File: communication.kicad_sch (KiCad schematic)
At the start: 17 parts, among them IC11 nRF52832-QFAA-R7, Y1 32MHz

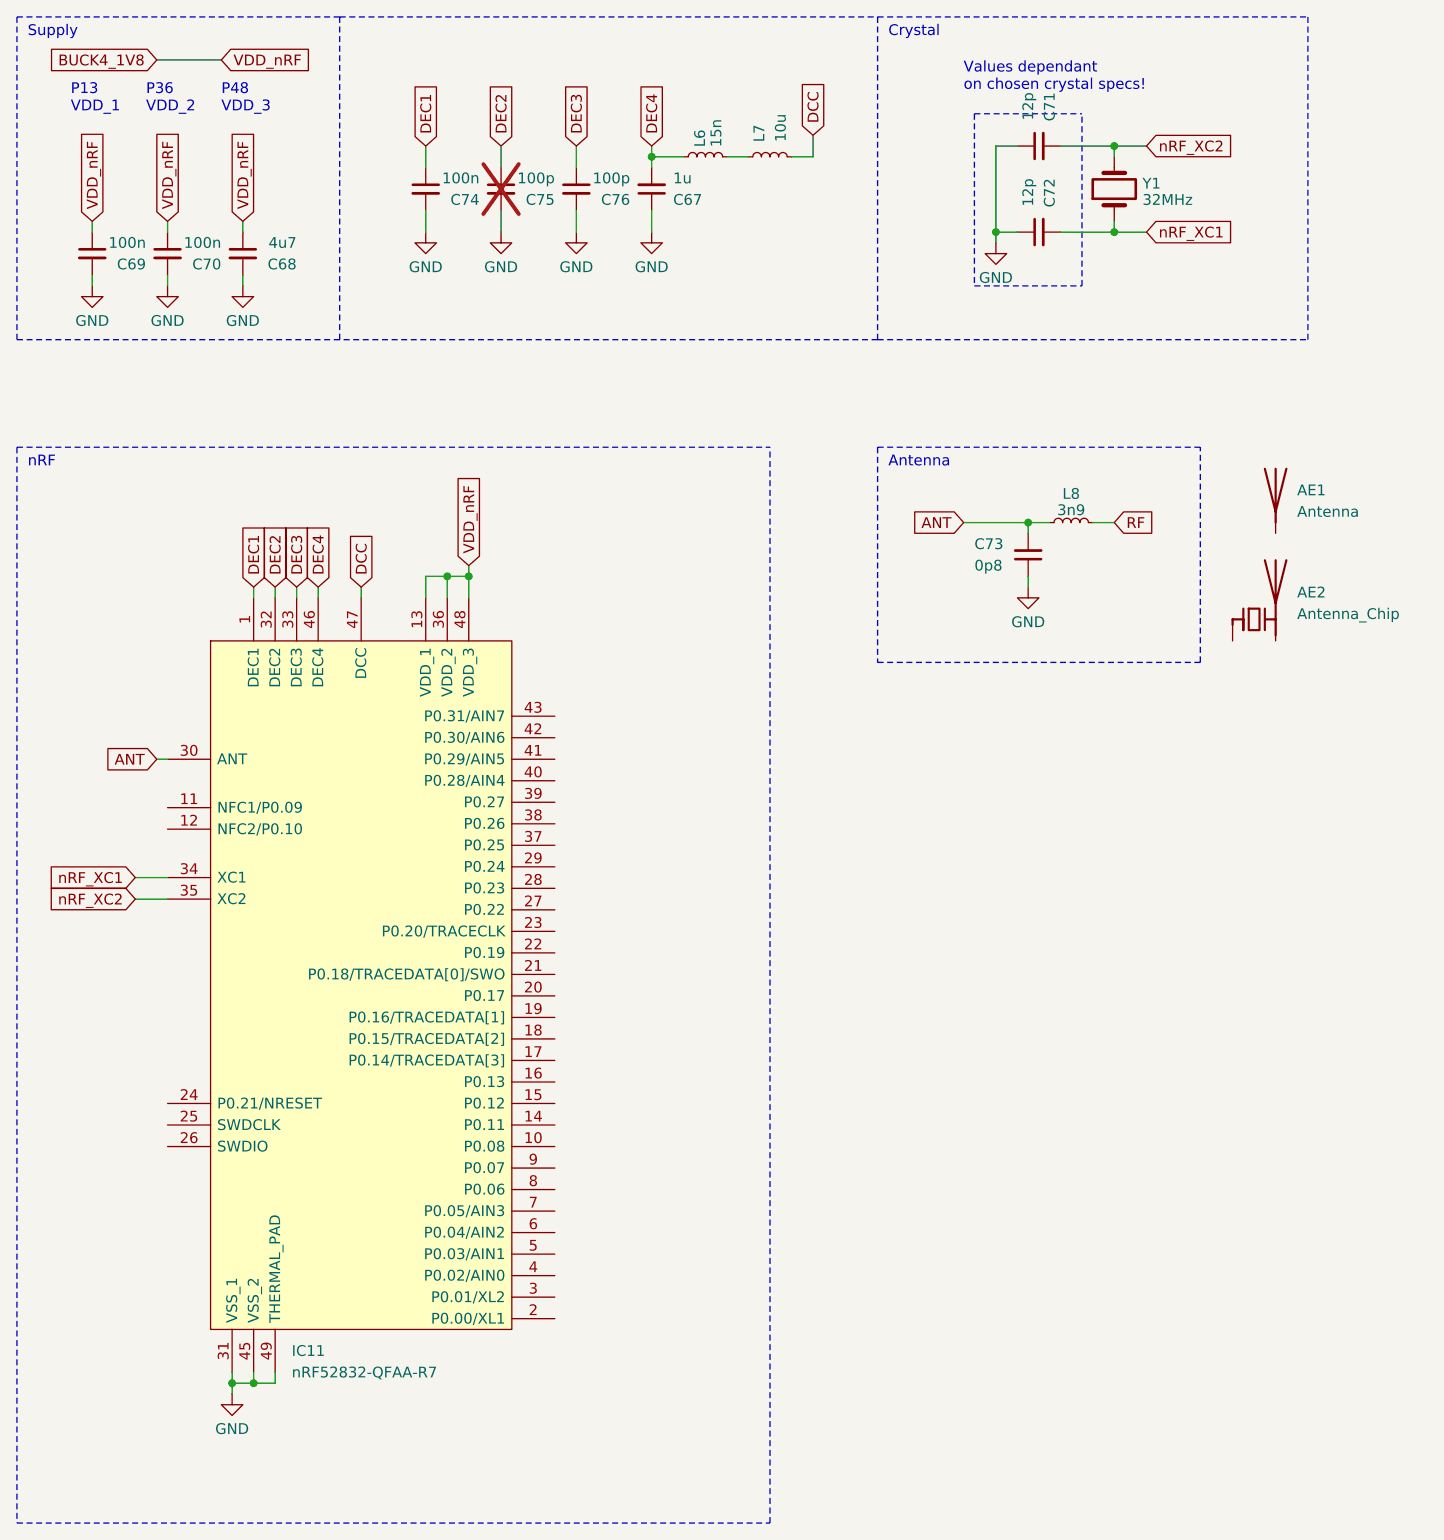
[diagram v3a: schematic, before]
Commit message: Added power to murata 1YN
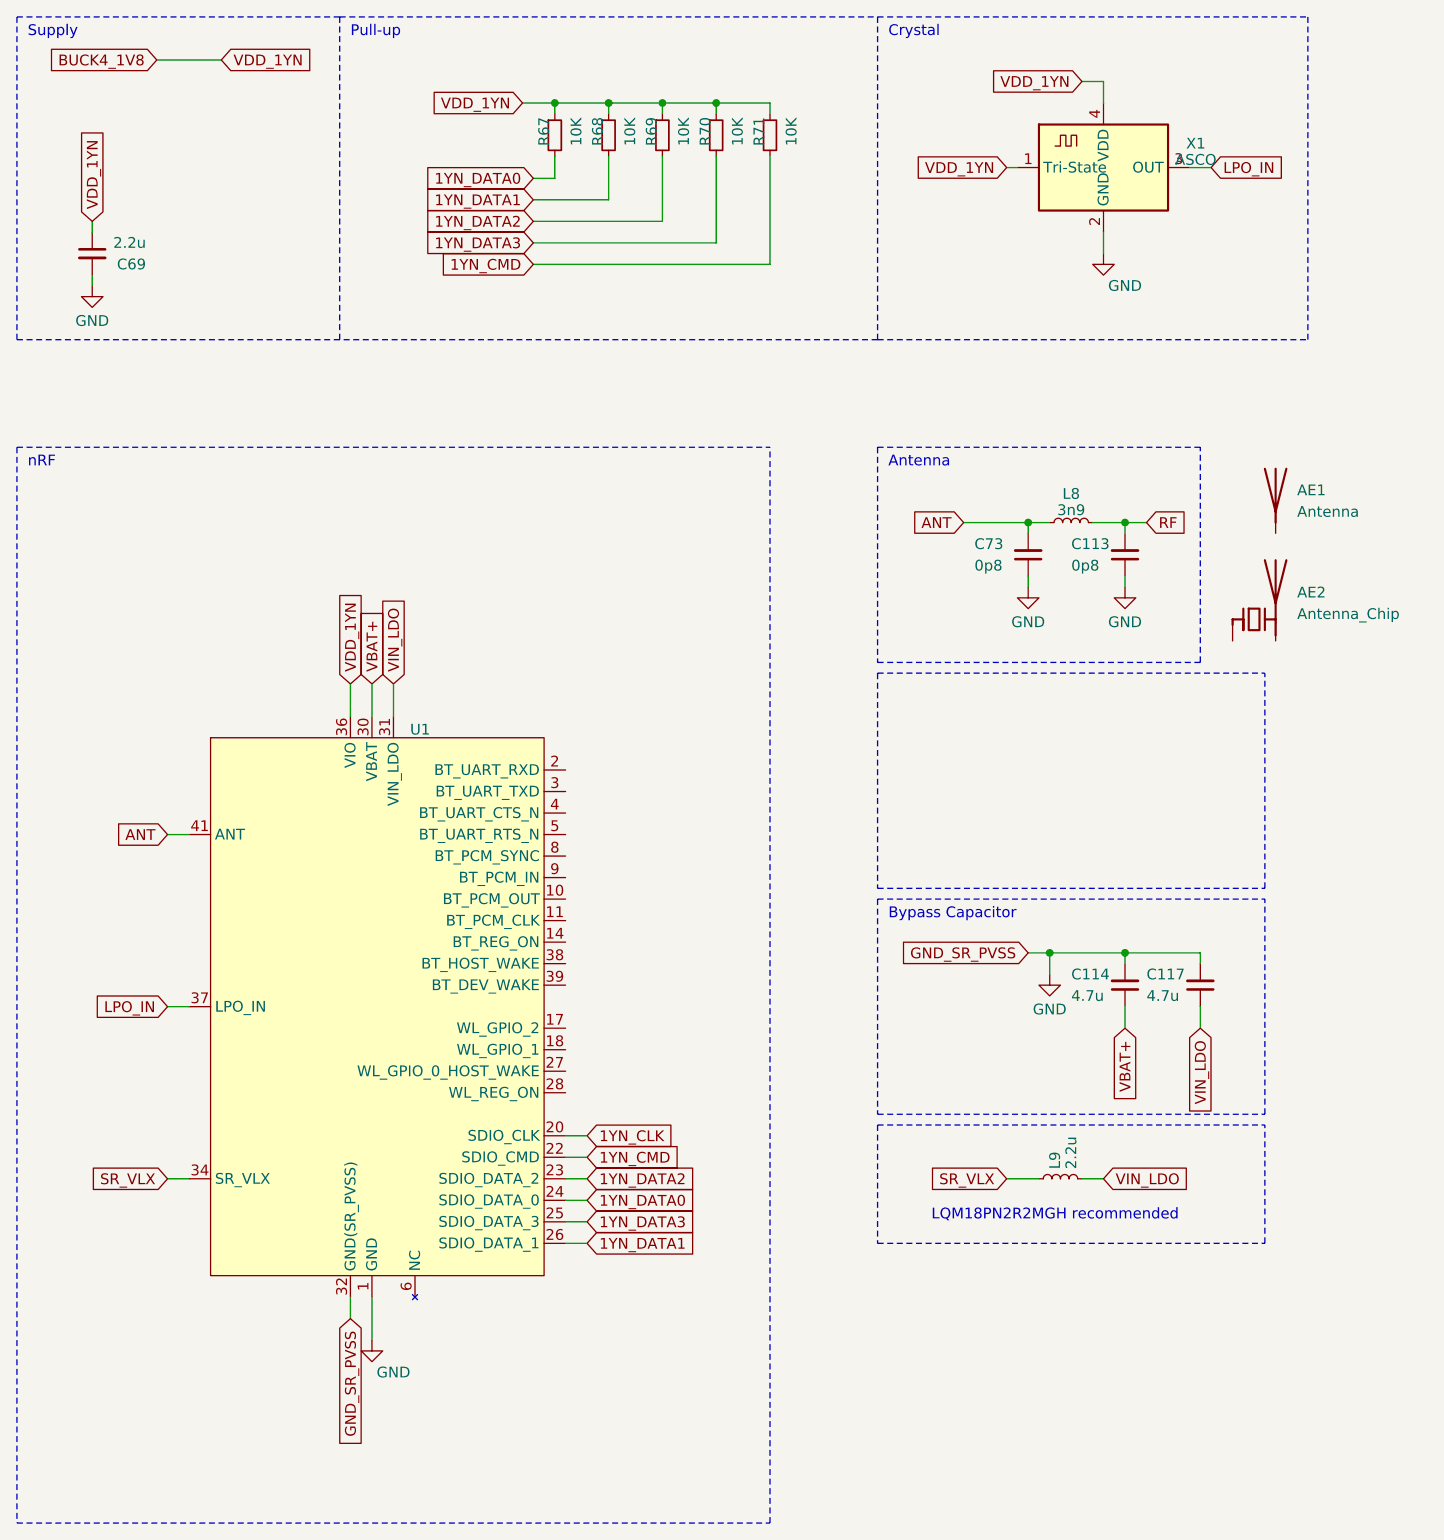
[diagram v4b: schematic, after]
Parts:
- removed C67: 1u, symbol Device:C_Small
- removed C68: 4u7, symbol Device:C_Small
- removed C70, C74: 100n, symbol Device:C_Small
- removed C71, C72: 12p, symbol Device:C_Small
- removed C75, C76: 100p, symbol Device:C_Small
- removed IC11: nRF52832-QFAA-R7, QFN40P600X600X90-49N-D, symbol ARMband:nRF52832-QFAA-R7
- removed L6: 15n, symbol Device:L_Small
- removed L7: 10u, symbol Device:L_Small
- removed Y1: 32MHz, symbol Device:Crystal
- added C113: 0p8, symbol Device:C_Small
- added C114, C117: 4.7u, symbol Device:C_Small
- added L9: 2.2u, symbol Device:L_Small
- added R67, R68, R69, R70, R71: 10K, symbol Device:R_Small
- added U1: ~, ARMband:Murata 1YN, symbol ARMband:Murata_1YN
- added X1: ASCO, Oscillator:Oscillator_SMD_Abracon_ASCO-4Pin_1.6x1.2mm, symbol Oscillator:ASCO
- C69: value 100n -> 2.2u
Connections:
- net ANT: now also U1.41 (ANT)
- net BUCK4_1V8: now also R67.1, R68.1, R69.1, R70.1, R71.1, U1.36 (VIO), X1.1 (Tri-State), X1.4 (VDD)
- net GND: now also C113.1, C114.2, C117.2, U1.1 (GND), U1.12 (GND), U1.19 (GND), U1.21 (GND), U1.29 (GND), U1.32 (GND(SR_PVSS)), U1.33 (GND(SR_PVSS)), U1.35 (GND), U1.40 (GND), U1.42 (GND), U1.43 (GND), U1.44 (GND), U1.45 (GND), U1.46 (GND), X1.2 (GND)
- net RF: now also C113.2
- new net: U1.13 (NC), U1.15 (NC), U1.16 (NC), U1.6 (NC), U1.7 (NC)
- new net 1YN_CLK: U1.20 (SDIO_CLK)
- new net 1YN_CMD: R71.2, U1.22 (SDIO_CMD)
- new net 1YN_DATA0: R67.2, U1.24 (SDIO_DATA_0)
- new net 1YN_DATA1: R68.2, U1.26 (SDIO_DATA_1)
- new net 1YN_DATA2: R69.2, U1.23 (SDIO_DATA_2)
- new net 1YN_DATA3: R70.2, U1.25 (SDIO_DATA_3)
- new net LPO_IN: U1.37 (LPO_IN), X1.3 (OUT)
- new net SR_VLX: L9.1, U1.34 (SR_VLX)
- new net VBAT+: C114.1, U1.30 (VBAT)
- new net VIN_LDO: C117.1, L9.2, U1.31 (VIN_LDO)
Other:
- note added: "Bypass Capacitor"
- note added: "LQM18PN2R2MGH recommended"
- note added: "Pull-up"
- note removed: "P13 VDD_1"
- note removed: "P36 VDD_2"
- note removed: "P48 VDD_3"
- note removed: "Values dependant on chosen crystal specs!"

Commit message: Added UART to 1YN
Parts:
- C113, C73: value 0p8 -> 3p979
- L8: value 3n9 -> 1n9894
- R67, R68, R69, R70, R71: footprint (none) -> Resistor_SMD:R_0201_0603Metric_Pad0.64x0.40mm_HandSolder
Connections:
- net BT_UART_RXD: now reaches U1.2 (BT_UART_RXD)
- net BT_UART_TXD: now reaches U1.3 (BT_UART_TXD)
- net BT_UART_CTS_N: now reaches U1.4 (BT_UART_CTS_N)
- net BT_UART_RTS_N: now reaches U1.5 (BT_UART_RTS_N)
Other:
- note added: "1YN"
- note removed: "nRF"
- moved on the sheet: AE1, AE2
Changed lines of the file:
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@@
+    (stroke (width 0) (type default))
+  )
+  (wire (pts (xy 77.47 109.22) (xy 80.01 109.22))
     (stroke (width 0) (type default))
   )
@@
     (stroke (width 0) (type default))
   )
+  (wire (pts (xy 77.47 101.6) (xy 80.01 101.6))
+    (stroke (width 0) (type default))
+  )
   (wire (pts (xy 151.13 30.48) (xy 153.67 30.48))
     (stroke (width 0) (type default))
@@
     (stroke (width 0) (type default))
   )
+  (wire (pts (xy 77.47 106.68) (xy 80.01 106.68))
+    (stroke (width 0) (type default))
+  )
   (wire (pts (xy 73.66 34.29) (xy 82.55 34.29))
     (stroke (width 0) (type default))
@@
   (polyline (pts (xy 101.6 190.5) (xy 101.6 63.5))
     (stroke (width 0) (type dash))
+  )
+  (wire (pts (xy 77.47 104.14) (xy 80.01 104.14))
+    (stroke (width 0) (type default))
   )
   (polyline (pts (xy 114.3 143.51) (xy 114.3 157.48))
@@
     (effects (font (size 1.27 1.27)) (justify left bottom))
   )
-  (text "nRF" (at 13.97 66.04 0)
+  (text "1YN" (at 13.97 66.04 0)
     (effects (font (size 1.27 1.27)) (justify left bottom))
   )
@@
     )
   )
+  (global_label "BT_UART_RTS_N" (shape input) (at 80.01 109.22 0) (fields_autoplaced)
+    (effects (font (size 1.27 1.27)) (justify left))
+    (property "Intersheetrefs" "${INTERSHEET_REFS}" (at 97.4905 109.22 0)
+      (effects (font (size 1.27 1.27)) (justify left) hide)
+    )
+  )
   (global_label "VIN_LDO" (shape input) (at 140.97 149.86 0) (fields_autoplaced)
     (effects (font (size 1.27 1.27)) (justify left))
@@
     )
   )
+  (global_label "BT_UART_CTS_N" (shape input) (at 80.01 106.68 0) (fields_autoplaced)
+    (effects (font (size 1.27 1.27)) (justify left))
+    (property "Intersheetrefs" "${INTERSHEET_REFS}" (at 97.4905 106.68 0)
+      (effects (font (size 1.27 1.27)) (justify left) hide)
+    )
+  )
   (global_label "VDD_1YN" (shape input) (at 36.83 17.78 0) (fields_autoplaced)
     (effects (font (size 1.27 1.27)) (justify left))
@@
     )
   )
+  (global_label "BT_UART_TXD" (shape input) (at 80.01 104.14 0) (fields_autoplaced)
+    (effects (font (size 1.27 1.27)) (justify left))
+    (property "Intersheetrefs" "${INTERSHEET_REFS}" (at 95.1924 104.14 0)
+      (effects (font (size 1.27 1.27)) (justify left) hide)
+    )
+  )
   (global_label "1YN_DATA1" (shape input) (at 80.01 157.48 0) (fields_autoplaced)
     (effects (font (size 1.27 1.27)) (justify left))
@@
     (property "Intersheetrefs" "${INTERSHEET_REFS}" (at 60.5337 34.29 0)
       (effects (font (size 1.27 1.27)) (justify right) hide)
+    )
+  )
+  (global_label "BT_UART_RXD" (shape input) (at 80.01 101.6 0) (fields_autoplaced)
+    (effects (font (size 1.27 1.27)) (justify left))
+    (property "Intersheetrefs" "${INTERSHEET_REFS}" (at 95.4948 101.6 0)
+      (effects (font (size 1.27 1.27)) (justify left) hide)
     )
   )
@@
       (effects (font (size 1.27 1.27)) (justify right))
     )
-    (property "Value" "0p8" (at 137.16 77.47 0)
+    (property "Value" "3p979" (at 135.89 77.47 0)
       (effects (font (size 1.27 1.27)) (justify right))
     )
@@
       (effects (font (size 1.27 1.27)) (justify left))
     )
-    (property "Footprint" "" (at 76.2 26.67 0)
+    (property "Footprint" "Resistor_SMD:R_0201_0603Metric_Pad0.64x0.40mm_HandSolder" (at 76.2 26.67 0)
       (effects (font (size 1.27 1.27)) hide)
     )
@@
     )
   )
-  (symbol (lib_id "Device:Antenna") (at 161.29 68.58 0) (unit 1)
+  (symbol (lib_id "Device:Antenna") (at 143.51 97.79 0) (unit 1)
     (in_bom yes) (on_board yes) (dnp no) (fields_autoplaced)
-    (property "Reference" "AE1" (at 163.83 68.58 0)
-      (effects (font (size 1.27 1.27)) (justify left))
-    )
-    (property "Value" "Antenna" (at 163.83 71.12 0)
-      (effects (font (size 1.27 1.27)) (justify left))
-    )
-    (property "Footprint" "" (at 161.29 68.58 0)
-      (effects (font (size 1.27 1.27)) hide)
-    )
-    (property "Datasheet" "~" (at 161.29 68.58 0)
+    (property "Reference" "AE1" (at 146.05 97.79 0)
+      (effects (font (size 1.27 1.27)) (justify left))
+    )
+    (property "Value" "Antenna" (at 146.05 100.33 0)
+      (effects (font (size 1.27 1.27)) (justify left))
+    )
+    (property "Footprint" "" (at 143.51 97.79 0)
+      (effects (font (size 1.27 1.27)) hide)
+    )
+    (property "Datasheet" "~" (at 143.51 97.79 0)
       (effects (font (size 1.27 1.27)) hide)
     )
@@
       (effects (font (size 1.27 1.27)) (justify left))
     )
-    (property "Footprint" "" (at 88.9 26.67 0)
+    (property "Footprint" "Resistor_SMD:R_0201_0603Metric_Pad0.64x0.40mm_HandSolder" (at 88.9 26.67 0)
       (effects (font (size 1.27 1.27)) hide)
     )
@@
       (effects (font (size 1.27 1.27)))
     )
-    (property "Value" "3n9" (at 137.16 70.9223 90)
+    (property "Value" "1n9894" (at 137.16 70.9223 90)
       (effects (font (size 1.27 1.27)))
     )
@@
       (effects (font (size 1.27 1.27)) (justify left))
     )
-    (property "Footprint" "" (at 101.6 26.67 0)
+    (property "Footprint" "Resistor_SMD:R_0201_0603Metric_Pad0.64x0.40mm_HandSolder" (at 101.6 26.67 0)
       (effects (font (size 1.27 1.27)) hide)
     )
@@
       (effects (font (size 1.27 1.27)) (justify left))
     )
-    (property "Footprint" "" (at 82.55 26.67 0)
+    (property "Footprint" "Resistor_SMD:R_0201_0603Metric_Pad0.64x0.40mm_HandSolder" (at 82.55 26.67 0)
       (effects (font (size 1.27 1.27)) hide)
     )
@@
     )
   )
-  (symbol (lib_id "Device:Antenna_Chip") (at 158.75 83.82 0) (unit 1)
+  (symbol (lib_id "Device:Antenna_Chip") (at 120.65 101.6 0) (unit 1)
     (in_bom yes) (on_board yes) (dnp no) (fields_autoplaced)
-    (property "Reference" "AE2" (at 163.83 80.645 0)
-      (effects (font (size 1.27 1.27)) (justify left))
-    )
-    (property "Value" "Antenna_Chip" (at 163.83 83.185 0)
-      (effects (font (size 1.27 1.27)) (justify left))
-    )
-    (property "Footprint" "" (at 156.21 79.375 0)
-      (effects (font (size 1.27 1.27)) hide)
-    )
-    (property "Datasheet" "~" (at 156.21 79.375 0)
+    (property "Reference" "AE2" (at 125.73 98.425 0)
+      (effects (font (size 1.27 1.27)) (justify left))
+    )
+    (property "Value" "Antenna_Chip" (at 125.73 100.965 0)
+      (effects (font (size 1.27 1.27)) (justify left))
+    )
+    (property "Footprint" "" (at 118.11 97.155 0)
+      (effects (font (size 1.27 1.27)) hide)
+    )
+    (property "Datasheet" "~" (at 118.11 97.155 0)
       (effects (font (size 1.27 1.27)) hide)
     )
@@
       (effects (font (size 1.27 1.27)) hide)
     )
-    (property "Datasheet" "" (at 46.99 129.54 0)
+    (property "Datasheet" "https://www.mouser.com/catalog/specsheets/Murata_LBEE5KL1YN-814.pdf" (at 46.99 129.54 0)
       (effects (font (size 1.27 1.27)) hide)
     )
@@
       (effects (font (size 1.27 1.27)) (justify left))
     )
-    (property "Footprint" "" (at 95.25 26.67 0)
+    (property "Footprint" "Resistor_SMD:R_0201_0603Metric_Pad0.64x0.40mm_HandSolder" (at 95.25 26.67 0)
       (effects (font (size 1.27 1.27)) hide)
     )
@@
       (effects (font (size 1.27 1.27)) (justify right))
     )
-    (property "Value" "0p8" (at 125.73 77.47 0)
+    (property "Value" "3p979" (at 124.46 77.47 0)
       (effects (font (size 1.27 1.27)) (justify right))
     )
